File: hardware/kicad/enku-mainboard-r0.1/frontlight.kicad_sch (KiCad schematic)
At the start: 5 parts

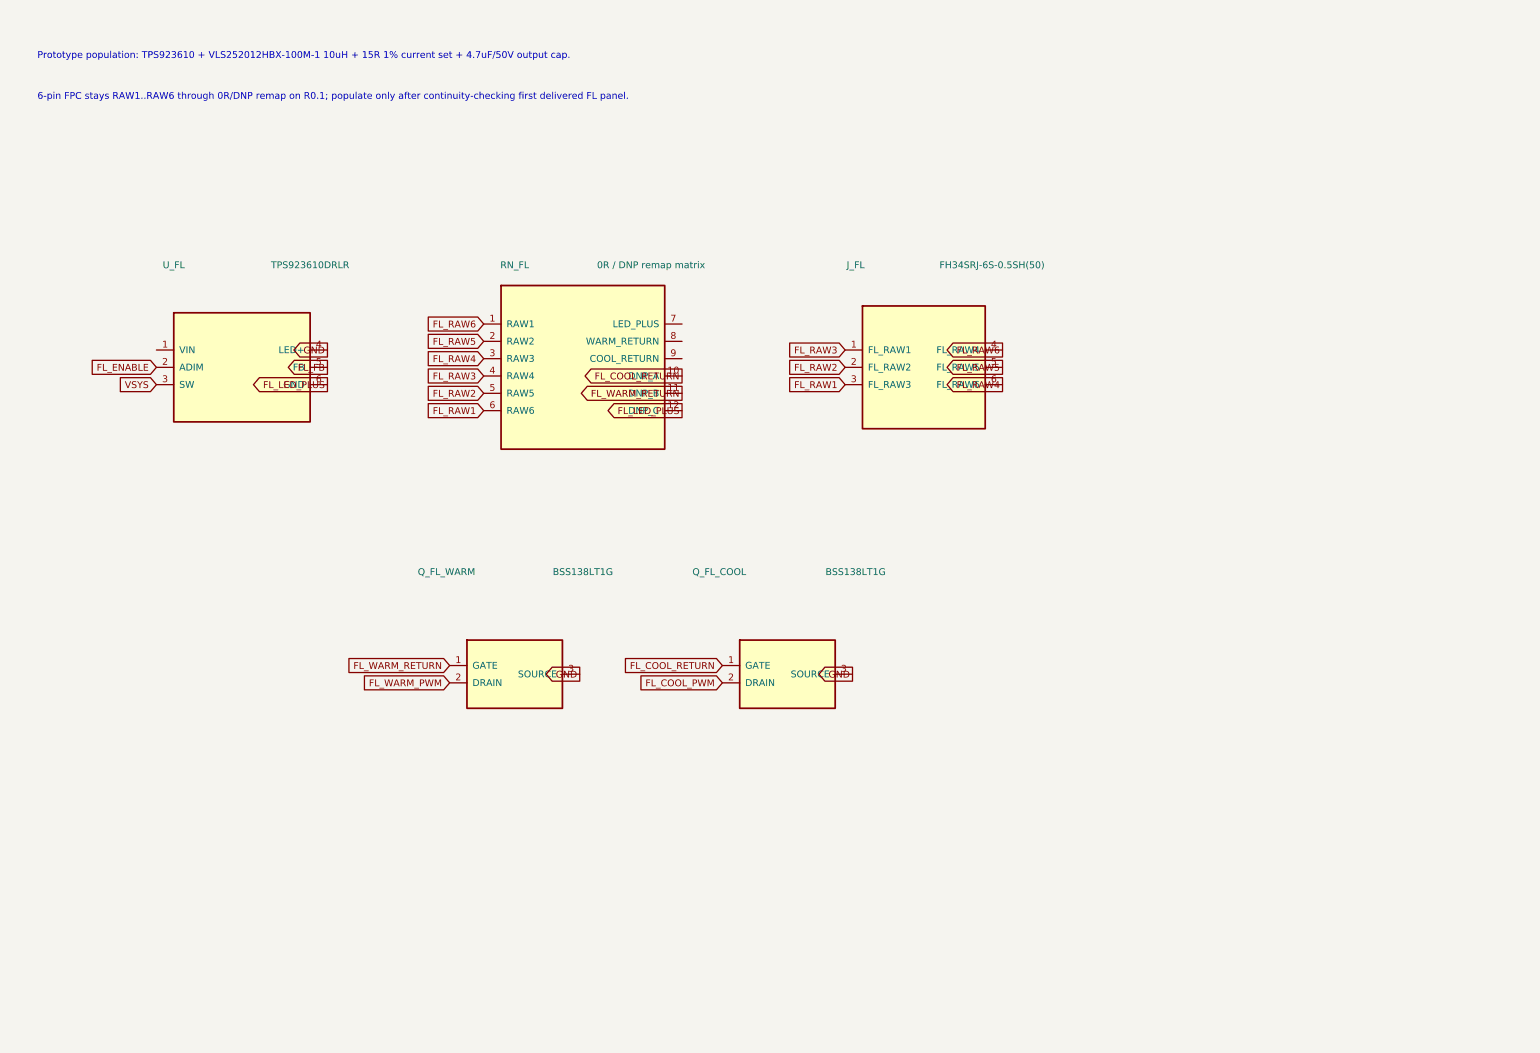
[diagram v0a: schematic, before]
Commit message: Expand Pro frontlight to exact TPS923610 circuit
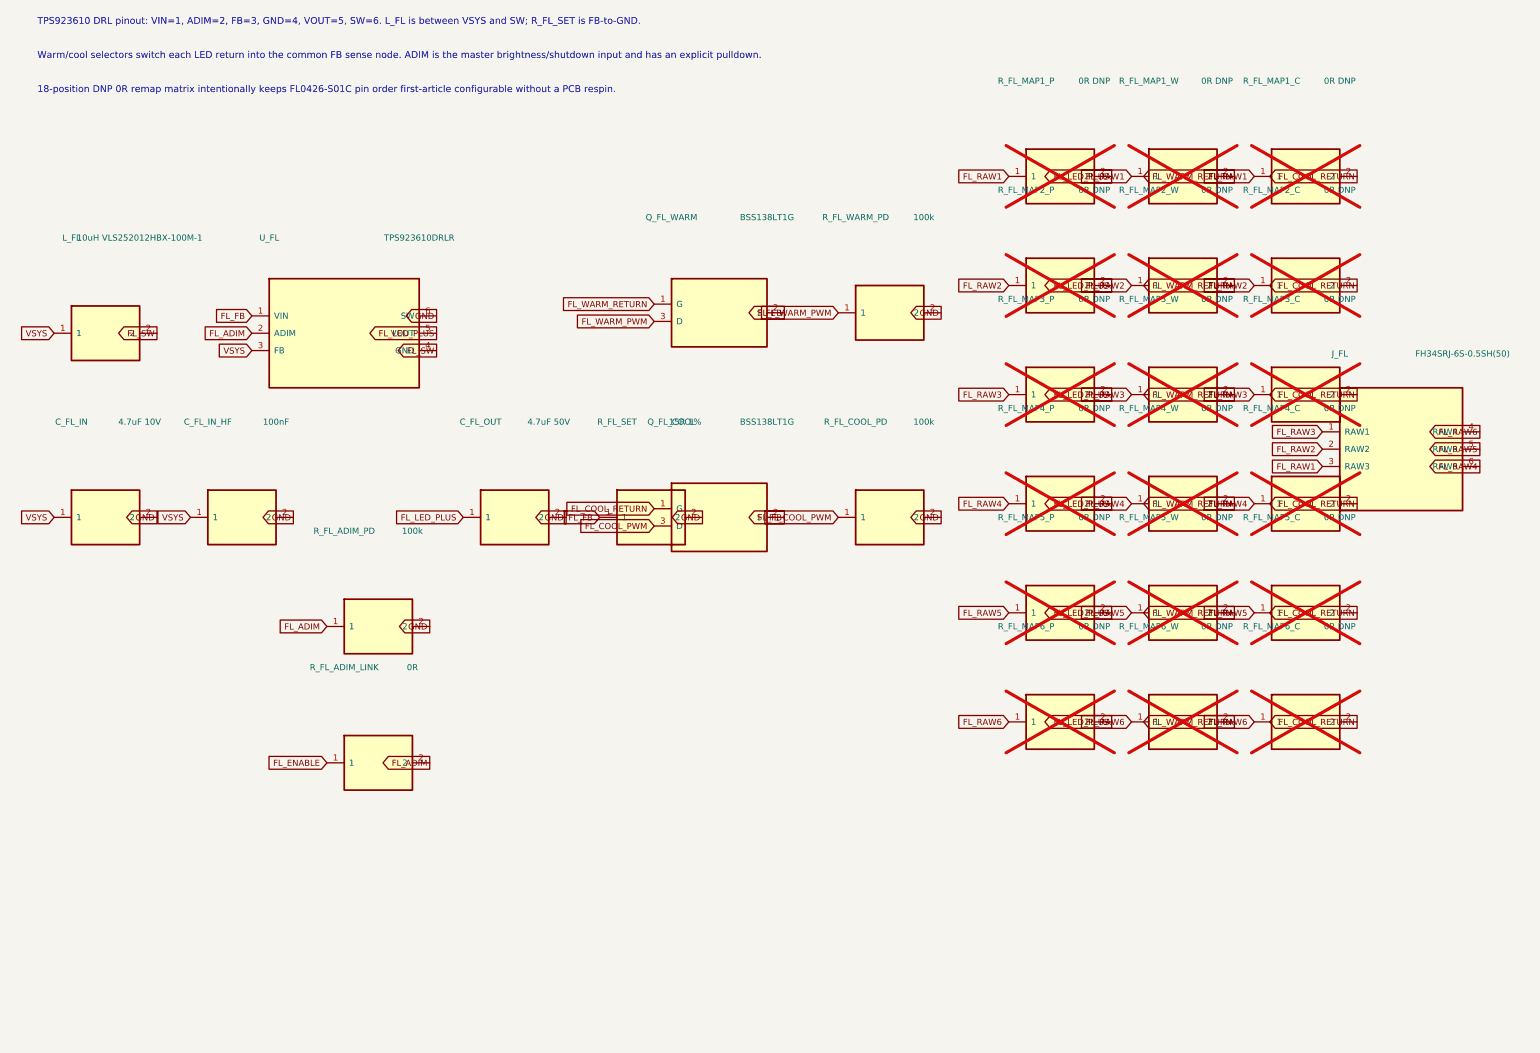
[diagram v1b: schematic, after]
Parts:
- removed J_FL: FH34SRJ-6S-0.5SH(50), ENKU:R0.1_FH34SRJ_6_DUAL_CONTACT_PLACEHOLDER, symbol ENKU:FL_FPC_6
- removed Q_FL_COOL, Q_FL_WARM: BSS138LT1G, Package_TO_SOT_SMD:SOT-23, symbol ENKU:FL_FET
- removed RN_FL: 0R / DNP remap matrix, symbol ENKU:FL_REMAP
- removed U_FL: TPS923610DRLR, ENKU:R0.1_TPS923610_SOT563_PLACEHOLDER, symbol ENKU:TPS923610_BLOCK
- added C_FL_IN: 4.7uF 10V, Capacitor_SMD:C_0805_2012Metric, symbol ENKU:C
- added C_FL_IN_HF: 100nF, Capacitor_SMD:C_0603_1608Metric, symbol ENKU:C
- added C_FL_OUT: 4.7uF 50V, Capacitor_SMD:C_0805_2012Metric, symbol ENKU:C
- added J_FL: FH34SRJ-6S-0.5SH(50), ENKU:R0.1_FH34SRJ_6_DUAL_CONTACT_PLACEHOLDER, symbol ENKU:FL_FPC6
- added L_FL: 10uH VLS252012HBX-100M-1, ENKU:TDK_VLS252012, symbol ENKU:L
- added Q_FL_COOL, Q_FL_WARM: BSS138LT1G, Package_TO_SOT_SMD:SOT-23, symbol ENKU:BSS138
- added R_FL_ADIM_LINK: 0R, Resistor_SMD:R_0603_1608Metric, symbol ENKU:R
- added R_FL_ADIM_PD, R_FL_COOL_PD, R_FL_WARM_PD: 100k, Resistor_SMD:R_0603_1608Metric, symbol ENKU:R
- added R_FL_MAP1_C, R_FL_MAP1_P, R_FL_MAP1_W, R_FL_MAP2_C, R_FL_MAP2_P, R_FL_MAP2_W, R_FL_MAP3_C, R_FL_MAP3_P, R_FL_MAP3_W, R_FL_MAP4_C, R_FL_MAP4_P, R_FL_MAP4_W, R_FL_MAP5_C, R_FL_MAP5_P, R_FL_MAP5_W, R_FL_MAP6_C, R_FL_MAP6_P, R_FL_MAP6_W: 0R DNP, Resistor_SMD:R_0402_1005Metric, symbol ENKU:R
- added R_FL_SET: 15R 1%, Resistor_SMD:R_0603_1608Metric, symbol ENKU:R
- added U_FL: TPS923610DRLR, Package_TO_SOT_SMD:SOT-563, symbol ENKU:TPS923610_DRL
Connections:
- net FL_COOL_PWM: now also Q_FL_COOL.3 (D), R_FL_COOL_PD.1
- net FL_COOL_RETURN: now also Q_FL_COOL.1 (G), R_FL_MAP1_C.2, R_FL_MAP2_C.2, R_FL_MAP3_C.2, R_FL_MAP4_C.2, R_FL_MAP5_C.2, R_FL_MAP6_C.2
- net FL_ENABLE: now also R_FL_ADIM_LINK.1
- net FL_FB: now also Q_FL_COOL.2 (S), Q_FL_WARM.2 (S), R_FL_SET.1, U_FL.1 (VIN)
- net FL_LED_PLUS: now also C_FL_OUT.1, R_FL_MAP1_P.2, R_FL_MAP2_P.2, R_FL_MAP3_P.2, R_FL_MAP4_P.2, R_FL_MAP5_P.2, R_FL_MAP6_P.2, U_FL.5 (VOUT)
- net FL_RAW1: now also J_FL.3 (RAW3), R_FL_MAP1_C.1, R_FL_MAP1_P.1, R_FL_MAP1_W.1
- net FL_RAW2: now also J_FL.2 (RAW2), R_FL_MAP2_C.1, R_FL_MAP2_P.1, R_FL_MAP2_W.1
- net FL_RAW3: now also J_FL.1 (RAW1), R_FL_MAP3_C.1, R_FL_MAP3_P.1, R_FL_MAP3_W.1
- net FL_RAW4: now also J_FL.6 (RAW6), R_FL_MAP4_C.1, R_FL_MAP4_P.1, R_FL_MAP4_W.1
- net FL_RAW5: now also J_FL.5 (RAW5), R_FL_MAP5_C.1, R_FL_MAP5_P.1, R_FL_MAP5_W.1
- net FL_RAW6: now also J_FL.4 (RAW4), R_FL_MAP6_C.1, R_FL_MAP6_P.1, R_FL_MAP6_W.1
- net FL_WARM_PWM: now also Q_FL_WARM.3 (D), R_FL_WARM_PD.1
- net FL_WARM_RETURN: now also Q_FL_WARM.1 (G), R_FL_MAP1_W.2, R_FL_MAP2_W.2, R_FL_MAP3_W.2, R_FL_MAP4_W.2, R_FL_MAP5_W.2, R_FL_MAP6_W.2
- net GND: now also C_FL_IN.2, C_FL_IN_HF.2, C_FL_OUT.2, R_FL_ADIM_PD.2, R_FL_COOL_PD.2, R_FL_SET.2, R_FL_WARM_PD.2, U_FL.6 (SW)
- net VSYS: now also C_FL_IN.1, C_FL_IN_HF.1, L_FL.1, U_FL.3 (FB)
- new net FL_ADIM: R_FL_ADIM_LINK.2, R_FL_ADIM_PD.1, U_FL.2 (ADIM)
- new net FL_SW: L_FL.2, U_FL.4 (GND)
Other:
- note added: "18-position DNP 0R remap matrix intentionally keeps FL0426-S01C pin order first-article configurable without a PCB respin."
- note added: "TPS923610 DRL pinout: VIN=1, ADIM=2, FB=3, GND=4, VOUT=5, SW=6. L_FL is between VSYS and SW; R_FL_SET is FB-to-GND."
- note added: "Warm/cool selectors switch each LED return into the common FB sense node. ADIM is the master brightness/shutdown input and has an explicit pulldown."
- note removed: "6-pin FPC stays RAW1..RAW6 through 0R/DNP remap on R0.1; populate only after continuity-checking first delivered FL panel."
- note removed: "Prototype population: TPS923610 + VLS252012HBX-100M-1 10uH + 15R 1% current set + 4.7uF/50V output cap."
- title: ENKU R0.1 — Frontlight -> ENKU Pro R0.1 — Frontlight

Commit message: Add R0.1 frontlight measurement test points
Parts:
- added TP_FL_FB: FL_FB, TestPoint:TestPoint_Pad_D1.5mm, symbol ENKU:TESTPOINT
- added TP_FL_LED_PLUS: FL_LED_PLUS, TestPoint:TestPoint_Pad_D1.5mm, symbol ENKU:TESTPOINT
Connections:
- net FL_FB: now also TP_FL_FB.1 (TP)
- net FL_LED_PLUS: now also TP_FL_LED_PLUS.1 (TP)
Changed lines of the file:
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@@
 	(text "Warm/cool selectors switch each LED return into the common FB sense node. ADIM is the master brightness/shutdown input and has an explicit pulldown." (exclude_from_sim no) (at 25 25 0) (effects (font (size 1.0 1.0)) (justify left bottom)))
 	(text "18-position DNP 0R remap matrix intentionally keeps FL0426-S01C pin order first-article configurable without a PCB respin." (exclude_from_sim no) (at 25 30 0) (effects (font (size 1.0 1.0)) (justify left bottom)))
+	(symbol (lib_id "ENKU:TESTPOINT") (at 55 165 0) (unit 1) (exclude_from_sim no) (in_bom yes) (on_board yes) (dnp no)
+		(property "Reference" "TP_FL_LED_PLUS" (at 55 162.46 0) (effects (font (size 0.9 0.9))))
+		(property "Value" "FL_LED_PLUS" (at 55 167.54 0) (effects (font (size 0.9 0.9))))
+		(property "Footprint" "TestPoint:TestPoint_Pad_D1.5mm" (at 55 165 0) (effects (font (size 0.9 0.9)) (hide yes)))
+		(property "Datasheet" "~" (at 55 165 0) (effects (font (size 0.9 0.9)) (hide yes)))
+		(property "Description" "ENKU R0.1 bring-up test point" (at 55 165 0) (effects (font (size 0.9 0.9)) (hide yes)))
+		(pin "1")
+		(instances (project "enku-mainboard-r0.1" (path "/10000000-0000-4000-8000-000000000001/10000000-0000-4000-8000-000000000040" (reference "TP_FL_LED_PLUS") (unit 1))))
+	)
+	(global_label "FL_LED_PLUS" (shape bidirectional) (at 51.19 165 0)
+		(effects (font (size 0.9 0.9)) (justify right bottom))
+)
+	(symbol (lib_id "ENKU:TESTPOINT") (at 95 165 0) (unit 1) (exclude_from_sim no) (in_bom yes) (on_board yes) (dnp no)
+		(property "Reference" "TP_FL_FB" (at 95 162.46 0) (effects (font (size 0.9 0.9))))
+		(property "Value" "FL_FB" (at 95 167.54 0) (effects (font (size 0.9 0.9))))
+		(property "Footprint" "TestPoint:TestPoint_Pad_D1.5mm" (at 95 165 0) (effects (font (size 0.9 0.9)) (hide yes)))
+		(property "Datasheet" "~" (at 95 165 0) (effects (font (size 0.9 0.9)) (hide yes)))
+		(property "Description" "ENKU R0.1 bring-up test point" (at 95 165 0) (effects (font (size 0.9 0.9)) (hide yes)))
+		(pin "1")
+		(instances (project "enku-mainboard-r0.1" (path "/10000000-0000-4000-8000-000000000001/10000000-0000-4000-8000-000000000040" (reference "TP_FL_FB") (unit 1))))
+	)
+	(global_label "FL_FB" (shape bidirectional) (at 91.19 165 0)
+		(effects (font (size 0.9 0.9)) (justify right bottom))
+)
 	(sheet_instances (path "/" (page "5")))
 )

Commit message: Bind frontlight parts to verified local footprints
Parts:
- J_FL: footprint ENKU:R0.1_FH34SRJ_6_DUAL_CONTACT_PLACEHOLDER -> ENKU:FH34SRJ-6S-0.5SH
- U_FL: footprint Package_TO_SOT_SMD:SOT-563 -> ENKU:TPS923610_DRL0006A
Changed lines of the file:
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@@
 		(property "Reference" "U_FL" (at 59 51 0) (effects (font (size 0.9 0.9))))
 		(property "Value" "TPS923610DRLR" (at 81 51 0) (effects (font (size 0.9 0.9))))
-		(property "Footprint" "Package_TO_SOT_SMD:SOT-563" (at 70 65 0) (effects (font (size 0.9 0.9)) (hide yes)))
+		(property "Footprint" "ENKU:TPS923610_DRL0006A" (at 70 65 0) (effects (font (size 0.9 0.9)) (hide yes)))
 		(property "Datasheet" "~" (at 70 65 0) (effects (font (size 0.9 0.9)) (hide yes)))
 		(property "Description" "TPS923610DRLR" (at 70 65 0) (effects (font (size 0.9 0.9)) (hide yes)))
@@
 		(property "Reference" "J_FL" (at 216 68 0) (effects (font (size 0.9 0.9))))
 		(property "Value" "FH34SRJ-6S-0.5SH(50)" (at 234 68 0) (effects (font (size 0.9 0.9))))
-		(property "Footprint" "ENKU:R0.1_FH34SRJ_6_DUAL_CONTACT_PLACEHOLDER" (at 225 82 0) (effects (font (size 0.9 0.9)) (hide yes)))
+		(property "Footprint" "ENKU:FH34SRJ-6S-0.5SH" (at 225 82 0) (effects (font (size 0.9 0.9)) (hide yes)))
 		(property "Datasheet" "~" (at 225 82 0) (effects (font (size 0.9 0.9)) (hide yes)))
 		(property "Description" "FH34SRJ-6S-0.5SH(50)" (at 225 82 0) (effects (font (size 0.9 0.9)) (hide yes)))
